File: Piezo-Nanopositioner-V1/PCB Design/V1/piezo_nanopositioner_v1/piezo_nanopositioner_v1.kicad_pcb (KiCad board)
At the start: 2 copper layers, 99 parts, among them J101 Conn_01x03_Pin, J2 RF2-04A-T-00-50-G, J201 Conn_01x10_Pin, J202 RF2-04A-T-00-50-G, J301 Conn_01x10_Pin, J302 RF2-04A-T-00-50-G, J401 Conn_01x10_Pin, J402 RF2-04A-T-00-50-G, U1 TDA2050, U2 DAC0800LCM, U201 TL431AIDBZR, U202 DAC0800LCM, U203 TDA2050, U3 TL431AIDBZR, U301 TL431AIDBZR, U302 DAC0800LCM, U303 TDA2050, U4 TL431AIDBZR, U401 TL431AIDBZR, U402 DAC0800LCM, U403 TDA2050

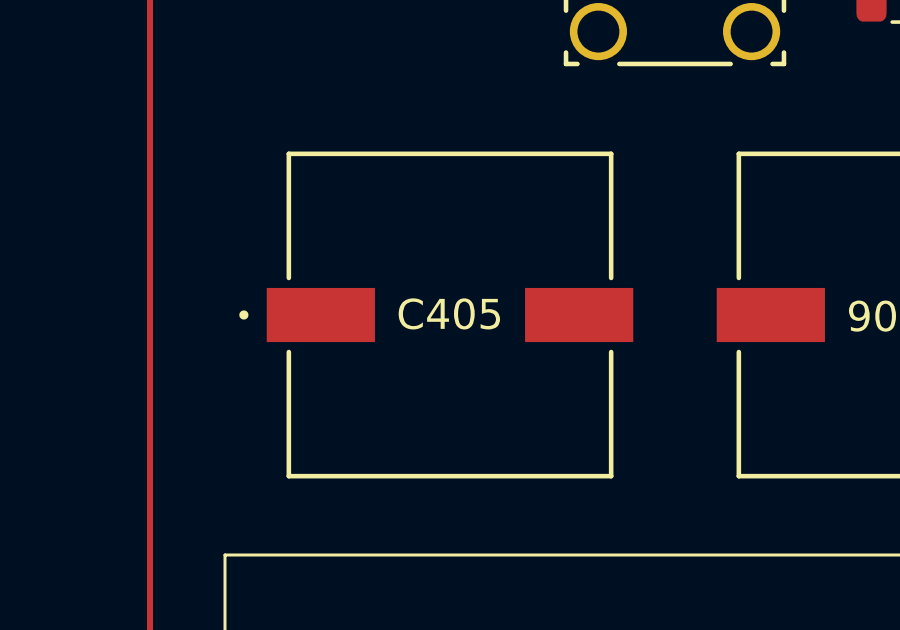
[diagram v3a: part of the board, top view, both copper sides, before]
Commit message: added heatsink to XYZ schematics, finalized BOM, minimal PCB layout done.
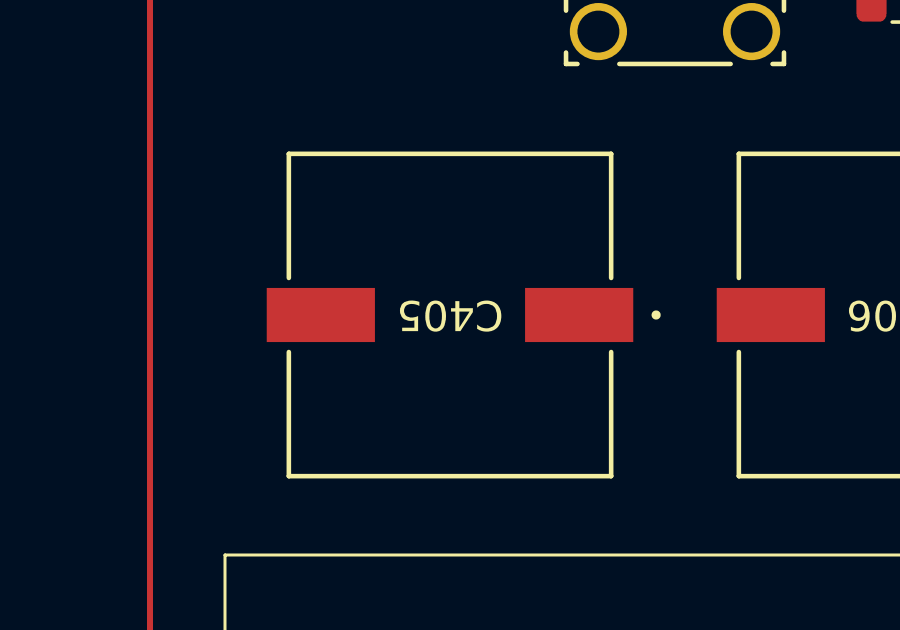
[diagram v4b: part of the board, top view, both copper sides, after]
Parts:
- turned C405 to 180 degrees
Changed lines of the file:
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@@
 		)
 		(property "Footprint" "Potentiometer_THT:TRIM_COM-09806"
-			(at 0 0 360)
+			(at 0 0 0)
 			(layer "F.Fab")
 			(hide yes)
@@
 		)
 		(property "Datasheet" ""
-			(at 0 0 360)
+			(at 0 0 0)
 			(layer "F.Fab")
 			(hide yes)
@@
 		)
 		(property "Description" "Trim-potentiometer"
-			(at 0 0 360)
+			(at 0 0 0)
 			(layer "F.Fab")
 			(hide yes)
@@
 	(footprint "Capacitor_THT:CAP_ZSU_G12_PAN"
 		(layer "F.Cu")
-		(at 106 60)
+		(at 106 60 180)
 		(tags "EEH-ZS1E471P ")
 		(property "Reference" "C405"
-			(at 0 0 0)
+			(at 0 0 180)
 			(unlocked yes)
 			(layer "F.SilkS")
@@
 		)
 		(property "Value" "470u"
-			(at 0 0 0)
+			(at 0 0 180)
 			(unlocked yes)
 			(layer "F.Fab")
@@
 		(attr smd)
 		(fp_line
-			(start -5.3721 -5.3721)
-			(end -5.3721 -1.23444)
+			(start 5.3721 5.3721)
+			(end 5.3721 1.23444)
 			(stroke
 				(width 0.1524)
@@
 		)
 		(fp_line
-			(start -5.3721 1.23444)
-			(end -5.3721 5.3721)
+			(start 5.3721 -1.23444)
+			(end 5.3721 -5.3721)
 			(stroke
 				(width 0.1524)
@@
 		)
 		(fp_line
-			(start -5.3721 5.3721)
-			(end 5.3721 5.3721)
+			(start 5.3721 -5.3721)
+			(end -5.3721 -5.3721)
 			(stroke
 				(width 0.1524)
@@
 		)
 		(fp_line
-			(start 5.3721 -5.3721)
-			(end -5.3721 -5.3721)
+			(start -5.3721 5.3721)
+			(end 5.3721 5.3721)
 			(stroke
 				(width 0.1524)
@@
 		)
 		(fp_line
-			(start 5.3721 -1.23444)
-			(end 5.3721 -5.3721)
+			(start -5.3721 1.23444)
+			(end -5.3721 5.3721)
 			(stroke
 				(width 0.1524)
@@
 		)
 		(fp_line
-			(start 5.3721 5.3721)
-			(end 5.3721 1.23444)
+			(start -5.3721 -5.3721)
+			(end -5.3721 -1.23444)
 			(stroke
 				(width 0.1524)
@@
 		)
 		(fp_line
-			(start -6.3627 -1.1557)
-			(end -5.4991 -1.1557)
+			(start 6.3627 1.1557)
+			(end 5.4991 1.1557)
 			(stroke
 				(width 0.1524)
@@
 		)
 		(fp_line
-			(start -6.3627 1.1557)
-			(end -6.3627 -1.1557)
+			(start 6.3627 -1.1557)
+			(end 6.3627 1.1557)
 			(stroke
 				(width 0.1524)
@@
 		)
 		(fp_line
-			(start -5.4991 -5.4991)
-			(end 5.4991 -5.4991)
+			(start 5.4991 5.4991)
+			(end -5.4991 5.4991)
 			(stroke
 				(width 0.1524)
@@
 		)
 		(fp_line
-			(start -5.4991 -1.1557)
-			(end -5.4991 -5.4991)
+			(start 5.4991 1.1557)
+			(end 5.4991 5.4991)
 			(stroke
 				(width 0.1524)
@@
 		)
 		(fp_line
-			(start -5.4991 1.1557)
-			(end -6.3627 1.1557)
+			(start 5.4991 -1.1557)
+			(end 6.3627 -1.1557)
 			(stroke
 				(width 0.1524)
@@
 		)
 		(fp_line
-			(start -5.4991 5.4991)
-			(end -5.4991 1.1557)
+			(start 5.4991 -5.4991)
+			(end 5.4991 -1.1557)
 			(stroke
 				(width 0.1524)
@@
 		)
 		(fp_line
-			(start 5.4991 -5.4991)
-			(end 5.4991 -1.1557)
+			(start -5.4991 5.4991)
+			(end -5.4991 1.1557)
 			(stroke
 				(width 0.1524)
@@
 		)
 		(fp_line
-			(start 5.4991 -1.1557)
-			(end 6.3627 -1.1557)
+			(start -5.4991 1.1557)
+			(end -6.3627 1.1557)
 			(stroke
 				(width 0.1524)
@@
 		)
 		(fp_line
-			(start 5.4991 1.1557)
-			(end 5.4991 5.4991)
+			(start -5.4991 -1.1557)
+			(end -5.4991 -5.4991)
 			(stroke
 				(width 0.1524)
@@
 		)
 		(fp_line
-			(start 5.4991 5.4991)
-			(end -5.4991 5.4991)
+			(start -5.4991 -5.4991)
+			(end 5.4991 -5.4991)
 			(stroke
 				(width 0.1524)
@@
 		)
 		(fp_line
-			(start 6.3627 -1.1557)
-			(end 6.3627 1.1557)
+			(start -6.3627 1.1557)
+			(end -6.3627 -1.1557)
 			(stroke
 				(width 0.1524)
@@
 		)
 		(fp_line
-			(start 6.3627 1.1557)
-			(end 5.4991 1.1557)
+			(start -6.3627 -1.1557)
+			(end -5.4991 -1.1557)
 			(stroke
 				(width 0.1524)
@@
 		)
 		(fp_line
-			(start -5.2451 -5.2451)
-			(end -5.2451 5.2451)
+			(start 5.2451 5.2451)
+			(end 5.2451 -5.2451)
 			(stroke
 				(width 0.0254)
@@
 		)
 		(fp_line
-			(start -5.2451 -2.62255)
-			(end -2.62255 -5.2451)
+			(start 5.2451 -5.2451)
+			(end -5.2451 -5.2451)
 			(stroke
 				(width 0.0254)
@@
 		)
 		(fp_line
-			(start -5.2451 2.62255)
-			(end -2.62255 5.2451)
+			(start -5.2451 5.2451)
+			(end 5.2451 5.2451)
 			(stroke
 				(width 0.0254)
@@
 		)
 		(fp_line
-			(start -5.2451 5.2451)
-			(end 5.2451 5.2451)
+			(start -5.2451 2.62255)
+			(end -2.62255 5.2451)
 			(stroke
 				(width 0.0254)
@@
 		)
 		(fp_line
-			(start 5.2451 -5.2451)
-			(end -5.2451 -5.2451)
+			(start -5.2451 -2.62255)
+			(end -2.62255 -5.2451)
 			(stroke
 				(width 0.0254)
@@
 		)
 		(fp_line
-			(start 5.2451 5.2451)
-			(end 5.2451 -5.2451)
+			(start -5.2451 -5.2451)
+			(end -5.2451 5.2451)
 			(stroke
 				(width 0.0254)
@@
 		)
 		(fp_text user "${REFERENCE}"
-			(at 0 0 0)
+			(at 0 0 180)
 			(unlocked yes)
 			(layer "F.Fab")
@@
 		)
 		(pad "1" smd rect
-			(at -4.3053 0)
+			(at -4.3053 0 180)
 			(size 3.6068 1.8034)
 			(layers "F.Cu" "F.Paste" "F.Mask")
@@
 		)
 		(pad "2" smd rect
-			(at 4.3053 0)
+			(at 4.3053 0 180)
 			(size 3.6068 1.8034)
 			(layers "F.Cu" "F.Paste" "F.Mask")
@@
 			(polygon
 				(pts
-					(xy 100.8057 54.8057) (xy 111.1943 54.8057) (xy 111.1943 59.0475) (xy 100.8057 59.0475)
+					(xy 108.4511 60.9525) (xy 103.5489 60.9525) (xy 103.5489 59.0475) (xy 108.4511 59.0475)
 				)
 			)
@@
 			(polygon
 				(pts
-					(xy 100.8057 60.9525) (xy 111.1943 60.9525) (xy 111.1943 65.1943) (xy 100.8057 65.1943)
+					(xy 111.1943 59.0475) (xy 100.8057 59.0475) (xy 100.8057 54.8057) (xy 111.1943 54.8057)
 				)
 			)
@@
 			(polygon
 				(pts
-					(xy 103.5489 59.0475) (xy 108.4511 59.0475) (xy 108.4511 60.9525) (xy 103.5489 60.9525)
+					(xy 111.1943 65.1943) (xy 100.8057 65.1943) (xy 100.8057 60.9525) (xy 111.1943 60.9525)
 				)
 			)
@@
 		(tags "capacitor")
 		(property "Reference" "C410"
-			(at -3.5 0 -0)
+			(at -3.5 0 0)
 			(layer "F.SilkS")
 			(effects
@@
 		)
 		(property "Value" "4.7n"
-			(at 0 -2.5 -360)
+			(at 0 -2.5 0)
 			(layer "F.Fab")
 			(effects
@@
 		)
 		(fp_text user "${REFERENCE}"
-			(at 0 0 360)
+			(at 0 0 0)
 			(layer "F.Fab")
 			(effects

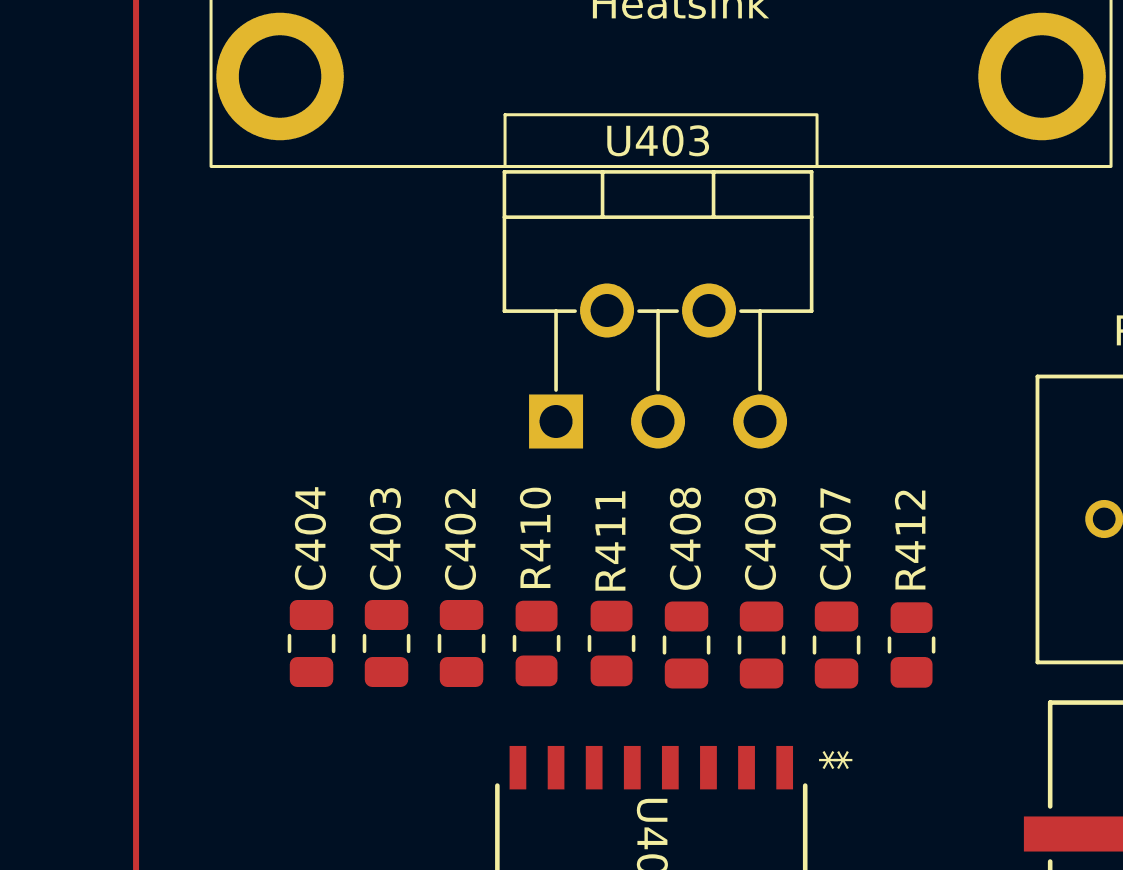
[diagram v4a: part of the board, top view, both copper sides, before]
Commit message: started working on op-amp simulation. The non-inverting part of the op-amp makes sense and works, still need to do some investigation about the zobel network.
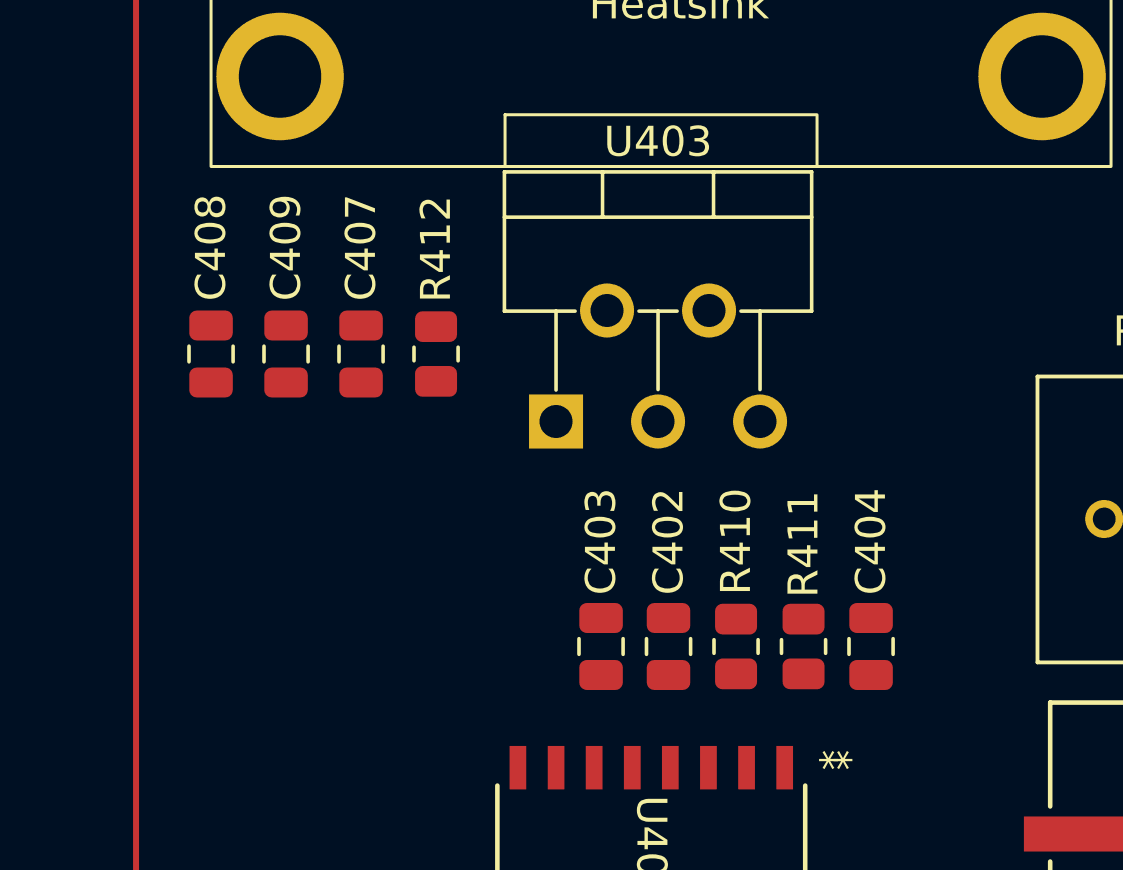
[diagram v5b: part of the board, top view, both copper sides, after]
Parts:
- moved C404 18.7 mm to (120.5, 96.0), turned to -90 degrees
- moved C407 18.6 mm to (103.5, 86.2)
- moved C408 18.6 mm to (98.5, 86.2)
- moved C409 18.6 mm to (101.0, 86.2)
- moved R412 18.6 mm to (106.0, 86.2)
- moved C403 7.15 mm to (111.5, 96.0)
- moved C402 6.90 mm to (113.8, 96.0)
- moved R410 6.65 mm to (116.0, 96.0), turned to 90 degrees
- moved R411 6.40 mm to (118.2, 96.0)
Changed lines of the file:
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@@
 	(footprint "Capacitor_SMD:C_0805_2012Metric"
 		(layer "F.Cu")
-		(at 119.35 95.95 90)
+		(at 103.5 86.25 90)
 		(descr "Capacitor SMD 0805 (2012 Metric), square (rectangular) end terminal, IPC_7351 nominal, (Body size source: IPC-SM-782 page 76, https://www.pcb-3d.com/wordpress/wp-content/uploads/ipc-sm-782a_amendment_1_and_2.pdf, https://docs.google.com/spreadsheets/d/1BsfQQcO9C6DZCsRaXUlFlo91Tg2WpOkGARC1WS5S8t0/edit?usp=sharing), generated with kicad-footprint-generator")
 		(tags "capacitor")
@@
 	(footprint "Capacitor_SMD:C_0805_2012Metric"
 		(layer "F.Cu")
-		(at 101.85 95.9 90)
+		(at 120.5 96 -90)
 		(descr "Capacitor SMD 0805 (2012 Metric), square (rectangular) end terminal, IPC_7351 nominal, (Body size source: IPC-SM-782 page 76, https://www.pcb-3d.com/wordpress/wp-content/uploads/ipc-sm-782a_amendment_1_and_2.pdf, https://docs.google.com/spreadsheets/d/1BsfQQcO9C6DZCsRaXUlFlo91Tg2WpOkGARC1WS5S8t0/edit?usp=sharing), generated with kicad-footprint-generator")
 		(tags "capacitor")
 		(property "Reference" "C404"
-			(at 3.5 0 90)
+			(at -3.5 0 90)
 			(layer "F.SilkS")
 			(effects
@@
 		)
 		(property "Footprint" "Capacitor_SMD:C_0805_2012Metric"
-			(at 0 0 90)
+			(at 0 0 -90)
 			(unlocked yes)
 			(layer "F.Fab")
@@
 		)
 		(property "Datasheet" ""
-			(at 0 0 90)
+			(at 0 0 -90)
 			(unlocked yes)
 			(layer "F.Fab")
@@
 		)
 		(property "Description" "Unpolarized capacitor"
-			(at 0 0 90)
+			(at 0 0 -90)
 			(unlocked yes)
 			(layer "F.Fab")
@@
 		(attr smd)
 		(fp_line
-			(start -0.261252 -0.735)
-			(end 0.261252 -0.735)
+			(start -0.261252 0.735)
+			(end 0.261252 0.735)
 			(stroke
 				(width 0.12)
@@
 		)
 		(fp_line
-			(start -0.261252 0.735)
-			(end 0.261252 0.735)
+			(start -0.261252 -0.735)
+			(end 0.261252 -0.735)
 			(stroke
 				(width 0.12)
@@
 		)
 		(fp_line
-			(start 1.7 -0.98)
-			(end 1.7 0.98)
+			(start -1.7 0.98)
+			(end -1.7 -0.98)
 			(stroke
 				(width 0.05)
@@
 		)
 		(fp_line
-			(start -1.7 -0.98)
-			(end 1.7 -0.98)
+			(start 1.7 0.98)
+			(end -1.7 0.98)
 			(stroke
 				(width 0.05)
@@
 		)
 		(fp_line
-			(start 1.7 0.98)
-			(end -1.7 0.98)
+			(start -1.7 -0.98)
+			(end 1.7 -0.98)
 			(stroke
 				(width 0.05)
@@
 		)
 		(fp_line
-			(start -1.7 0.98)
-			(end -1.7 -0.98)
+			(start 1.7 -0.98)
+			(end 1.7 0.98)
 			(stroke
 				(width 0.05)
@@
 		)
 		(fp_line
-			(start 1 -0.625)
-			(end 1 0.625)
+			(start -1 0.625)
+			(end -1 -0.625)
 			(stroke
 				(width 0.1)
@@
 		)
 		(fp_line
-			(start -1 -0.625)
-			(end 1 -0.625)
+			(start 1 0.625)
+			(end -1 0.625)
 			(stroke
 				(width 0.1)
@@
 		)
 		(fp_line
-			(start 1 0.625)
-			(end -1 0.625)
+			(start -1 -0.625)
+			(end 1 -0.625)
 			(stroke
 				(width 0.1)
@@
 		)
 		(fp_line
-			(start -1 0.625)
-			(end -1 -0.625)
+			(start 1 -0.625)
+			(end 1 0.625)
 			(stroke
 				(width 0.1)
@@
 		)
 		(pad "1" smd roundrect
-			(at -0.95 0 90)
+			(at -0.95 0 270)
 			(size 1 1.45)
 			(layers "F.Cu" "F.Paste" "F.Mask")
@@
 		)
 		(pad "2" smd roundrect
-			(at 0.95 0 90)
+			(at 0.95 0 270)
 			(size 1 1.45)
 			(layers "F.Cu" "F.Paste" "F.Mask")
@@
 	(footprint "Resistor_SMD:R_0805_2012Metric"
 		(layer "F.Cu")
-		(at 109.35 95.9 -90)
+		(at 116 96 90)
 		(descr "Resistor SMD 0805 (2012 Metric), square (rectangular) end terminal, IPC_7351 nominal, (Body size source: IPC-SM-782 page 72, https://www.pcb-3d.com/wordpress/wp-content/uploads/ipc-sm-782a_amendment_1_and_2.pdf), generated with kicad-footprint-generator")
 		(tags "resistor")
 		(property "Reference" "R410"
-			(at -3.5 0 90)
+			(at 3.5 0 90)
 			(layer "F.SilkS")
 			(effects
@@
 		)
 		(property "Footprint" "Resistor_SMD:R_0805_2012Metric"
-			(at 0 0 -90)
+			(at 0 0 90)
 			(unlocked yes)
 			(layer "F.Fab")
@@
 		)
 		(property "Datasheet" ""
-			(at 0 0 -90)
+			(at 0 0 90)
 			(unlocked yes)
 			(layer "F.Fab")
@@
 		)
 		(property "Description" "Resistor"
-			(at 0 0 -90)
+			(at 0 0 90)
 			(unlocked yes)
 			(layer "F.Fab")
@@
 		(attr smd)
 		(fp_line
-			(start -0.227064 0.735)
-			(end 0.227064 0.735)
+			(start -0.227064 -0.735)
+			(end 0.227064 -0.735)
 			(stroke
 				(width 0.12)
@@
 		)
 		(fp_line
-			(start -0.227064 -0.735)
-			(end 0.227064 -0.735)
+			(start -0.227064 0.735)
+			(end 0.227064 0.735)
 			(stroke
 				(width 0.12)
@@
 		)
 		(fp_line
-			(start -1.68 0.95)
-			(end -1.68 -0.95)
+			(start 1.68 -0.95)
+			(end 1.68 0.95)
 			(stroke
 				(width 0.05)
@@
 		)
 		(fp_line
-			(start 1.68 0.95)
-			(end -1.68 0.95)
+			(start -1.68 -0.95)
+			(end 1.68 -0.95)
 			(stroke
 				(width 0.05)
@@
 		)
 		(fp_line
-			(start -1.68 -0.95)
-			(end 1.68 -0.95)
+			(start 1.68 0.95)
+			(end -1.68 0.95)
 			(stroke
 				(width 0.05)
@@
 		)
 		(fp_line
-			(start 1.68 -0.95)
-			(end 1.68 0.95)
+			(start -1.68 0.95)
+			(end -1.68 -0.95)
 			(stroke
 				(width 0.05)
@@
 		)
 		(fp_line
-			(start -1 0.625)
-			(end -1 -0.625)
+			(start 1 -0.625)
+			(end 1 0.625)
 			(stroke
 				(width 0.1)
@@
 		)
 		(fp_line
-			(start 1 0.625)
-			(end -1 0.625)
+			(start -1 -0.625)
+			(end 1 -0.625)
 			(stroke
 				(width 0.1)
@@
 		)
 		(fp_line
-			(start -1 -0.625)
-			(end 1 -0.625)
+			(start 1 0.625)
+			(end -1 0.625)
 			(stroke
 				(width 0.1)
@@
 		)
 		(fp_line
-			(start 1 -0.625)
-			(end 1 0.625)
+			(start -1 0.625)
+			(end -1 -0.625)
 			(stroke
 				(width 0.1)
@@
 		)
 		(pad "1" smd roundrect
-			(at -0.9125 0 270)
+			(at -0.9125 0 90)
 			(size 1.025 1.4)
 			(layers "F.Cu" "F.Paste" "F.Mask")
@@
 		)
 		(pad "2" smd roundrect
-			(at 0.9125 0 270)
+			(at 0.9125 0 90)
 			(size 1.025 1.4)
 			(layers "F.Cu" "F.Paste" "F.Mask")
@@
 	(footprint "Capacitor_SMD:C_0805_2012Metric"
 		(layer "F.Cu")
-		(at 114.35 95.95 90)
+		(at 98.5 86.25 90)
 		(descr "Capacitor SMD 0805 (2012 Metric), square (rectangular) end terminal, IPC_7351 nominal, (Body size source: IPC-SM-782 page 76, https://www.pcb-3d.com/wordpress/wp-content/uploads/ipc-sm-782a_amendment_1_and_2.pdf, https://docs.google.com/spreadsheets/d/1BsfQQcO9C6DZCsRaXUlFlo91Tg2WpOkGARC1WS5S8t0/edit?usp=sharing), generated with kicad-footprint-generator")
 		(tags "capacitor")
@@
 	(footprint "Resistor_SMD:R_0805_2012Metric"
 		(layer "F.Cu")
-		(at 121.85 95.95 90)
+		(at 106 86.25 90)
 		(descr "Resistor SMD 0805 (2012 Metric), square (rectangular) end terminal, IPC_7351 nominal, (Body size source: IPC-SM-782 page 72, https://www.pcb-3d.com/wordpress/wp-content/uploads/ipc-sm-782a_amendment_1_and_2.pdf), generated with kicad-footprint-generator")
 		(tags "resistor")
@@
 	(footprint "Capacitor_SMD:C_0805_2012Metric"
 		(layer "F.Cu")
-		(at 116.85 95.95 -90)
+		(at 101 86.25 -90)
 		(descr "Capacitor SMD 0805 (2012 Metric), square (rectangular) end terminal, IPC_7351 nominal, (Body size source: IPC-SM-782 page 76, https://www.pcb-3d.com/wordpress/wp-content/uploads/ipc-sm-782a_amendment_1_and_2.pdf, https://docs.google.com/spreadsheets/d/1BsfQQcO9C6DZCsRaXUlFlo91Tg2WpOkGARC1WS5S8t0/edit?usp=sharing), generated with kicad-footprint-generator")
 		(tags "capacitor")
@@
 	(footprint "Capacitor_SMD:C_0805_2012Metric"
 		(layer "F.Cu")
-		(at 106.85 95.9 90)
+		(at 113.75 96 90)
 		(descr "Capacitor SMD 0805 (2012 Metric), square (rectangular) end terminal, IPC_7351 nominal, (Body size source: IPC-SM-782 page 76, https://www.pcb-3d.com/wordpress/wp-content/uploads/ipc-sm-782a_amendment_1_and_2.pdf, https://docs.google.com/spreadsheets/d/1BsfQQcO9C6DZCsRaXUlFlo91Tg2WpOkGARC1WS5S8t0/edit?usp=sharing), generated with kicad-footprint-generator")
 		(tags "capacitor")
@@
 	(footprint "Capacitor_SMD:C_0805_2012Metric"
 		(layer "F.Cu")
-		(at 104.35 95.9 -90)
+		(at 111.5 96 -90)
 		(descr "Capacitor SMD 0805 (2012 Metric), square (rectangular) end terminal, IPC_7351 nominal, (Body size source: IPC-SM-782 page 76, https://www.pcb-3d.com/wordpress/wp-content/uploads/ipc-sm-782a_amendment_1_and_2.pdf, https://docs.google.com/spreadsheets/d/1BsfQQcO9C6DZCsRaXUlFlo91Tg2WpOkGARC1WS5S8t0/edit?usp=sharing), generated with kicad-footprint-generator")
 		(tags "capacitor")
@@
 	(footprint "Resistor_SMD:R_0805_2012Metric"
 		(layer "F.Cu")
-		(at 111.85 95.9 90)
+		(at 118.25 96 90)
 		(descr "Resistor SMD 0805 (2012 Metric), square (rectangular) end terminal, IPC_7351 nominal, (Body size source: IPC-SM-782 page 72, https://www.pcb-3d.com/wordpress/wp-content/uploads/ipc-sm-782a_amendment_1_and_2.pdf), generated with kicad-footprint-generator")
 		(tags "resistor")
